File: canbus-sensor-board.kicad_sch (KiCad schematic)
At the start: 48 parts, among them J1 CAN IO, J2 CAN Term, J3 POWER IN, J4 Debug, J5 I2C2 IO, J6 I2C1 IO, Q1 2N7002, Q2 2N7002, Q3 2N7002, Q4 2N7002, SW1 Reset, SW2 Boot, U1 MCP2551-I-SN, U3 AMS1117-3.3, U4 STM32F103C8Tx

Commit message: Update board to rev 3 (we do not talk about rev 2)
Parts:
- removed J4: Debug, Connector_PinHeader_2.54mm:PinHeader_1x04_P2.54mm_Vertical, symbol Connector:Conn_01x04_Pin
- removed SW1: Reset, Button_Switch_SMD:SW_Push_1P1T_XKB_TS-1187A, symbol Switch:SW_SPST
- removed SW2: Boot, Button_Switch_SMD:SW_Push_1P1T_XKB_TS-1187A, symbol Switch:SW_SPST
- added J10, J11, J4, J7, J9: Conn_01x01, Connector_Wire:SolderWirePad_1x01_SMD_1x2mm, symbol Connector_Generic:Conn_01x01
- added J8: Conn_ARM_SWD_TagConnect_TC2030-NL, Connector:Tag-Connect_TC2030-IDC-NL_2x03_P1.27mm_Vertical, symbol Connector:Conn_ARM_SWD_TagConnect_TC2030-NL
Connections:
- net +3.3V: now also R3.2, J11.1 (Pin_1), J8.1 (VCC); no longer R3.1
- net +5V: now also J4.1 (Pin_1)
- net BOOT: now also J7.1 (Pin_1)
- net CAN_RX: now also U4.45 (PB8); no longer U4.29 (PA8)
- net CAN_TX: now also U4.46 (PB9); no longer U4.30 (PA9)
- net DEBUG_LED1: now also U4.38 (PA15); no longer U4.37 (PA14)
- net GND: now also J10.1 (Pin_1), J8.5 (GND)
- net NRST: now also R3.1, J8.3 (~{RESET}), J9.1 (Pin_1); no longer R3.2
- net SWDIO: now reaches U4.34 (PA13)
- net SWDIO: now also J8.2 (SWDIO)
- net SWO: now reaches U4.39 (PB3)
- net SWO: now also J8.6 (SWO)
- net SYS_SWCLK: no longer names the net of U4.32 (PA11)
- net SYS_SWDIO: no longer names the net of U4.31 (PA10)
- new net SWCLK: J8.4 (SWCLK), U4.37 (PA14)
- no-connect marks 27 -> 26

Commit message: Switch to MOSFETs with lower Vgs thresholds
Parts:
- removed Q1, Q2, Q3, Q4: 2N7002, Package_TO_SOT_SMD:SOT-23, symbol Transistor_FET:2N7002
- added Q1, Q2, Q3, Q4: AO3400A, Package_TO_SOT_SMD:SOT-23, symbol Transistor_FET:AO3400A
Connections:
- net +3.3V: now also Q1.1 (G), Q2.1 (G), Q3.1 (G), Q4.1 (G)
- net I2C1_SCL: now also Q1.2 (S)
- net I2C1_SCL_5V: now also Q1.3 (D)
- net I2C1_SDA: now also Q2.2 (S)
- net I2C1_SDA_5V: now also Q2.3 (D)
- net I2C2_SCL: now also Q3.2 (S)
- net I2C2_SCL_5V: now also Q3.3 (D)
- net I2C2_SDA: now also Q4.2 (S)
- net I2C2_SDA_5V: now also Q4.3 (D)

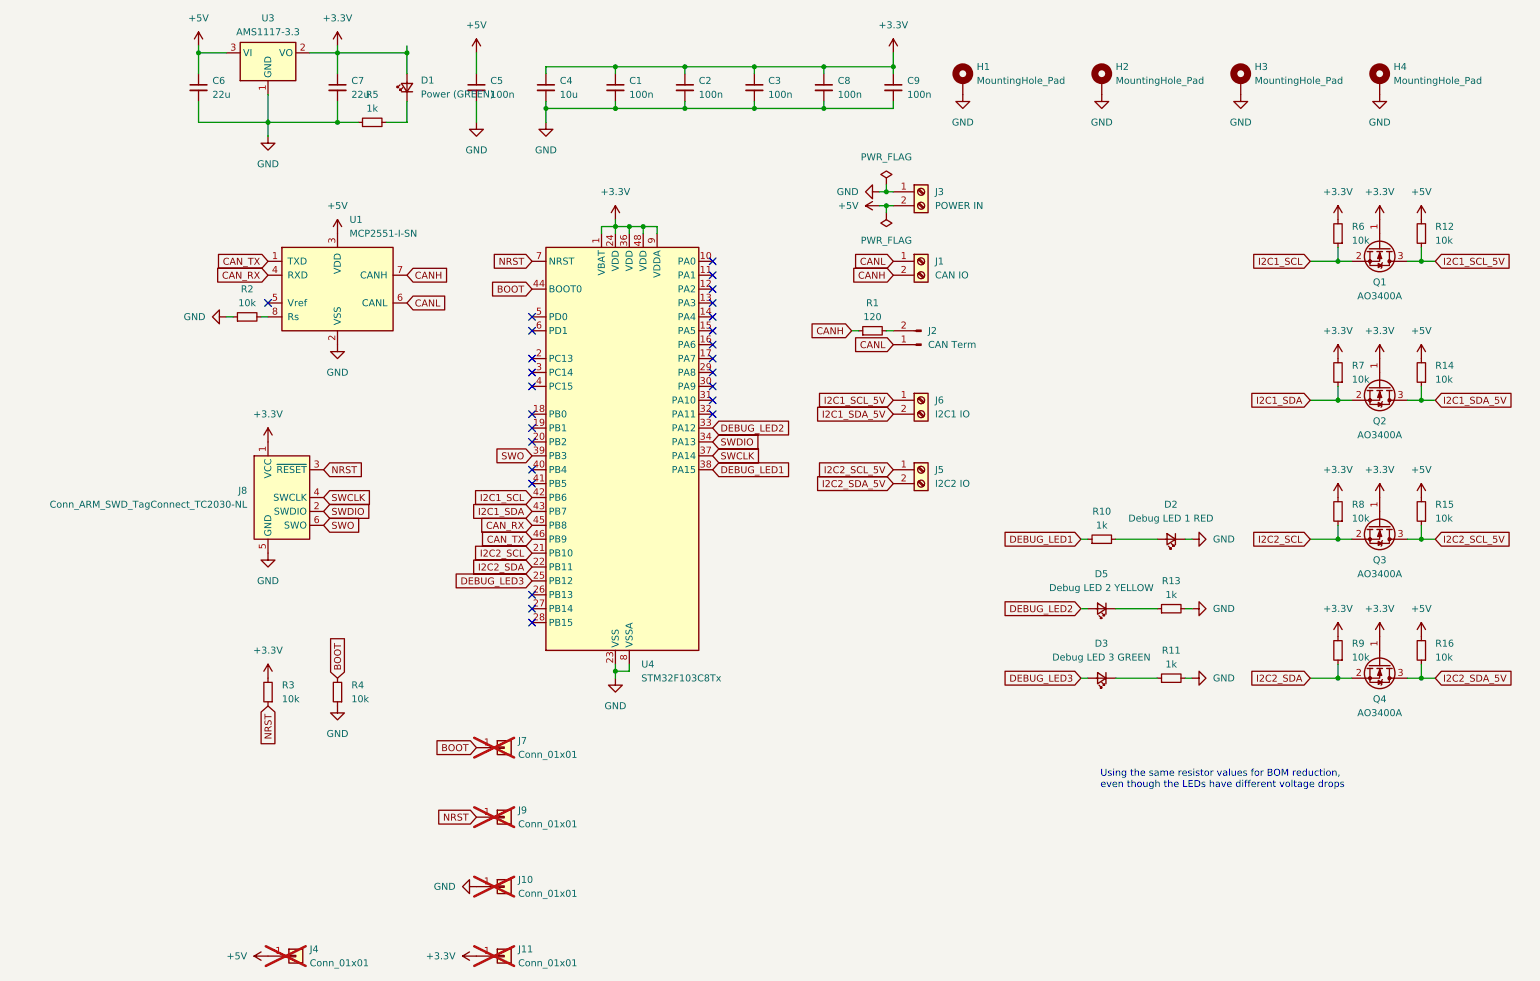
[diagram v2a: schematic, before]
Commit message: Further tweak rev4 of the board
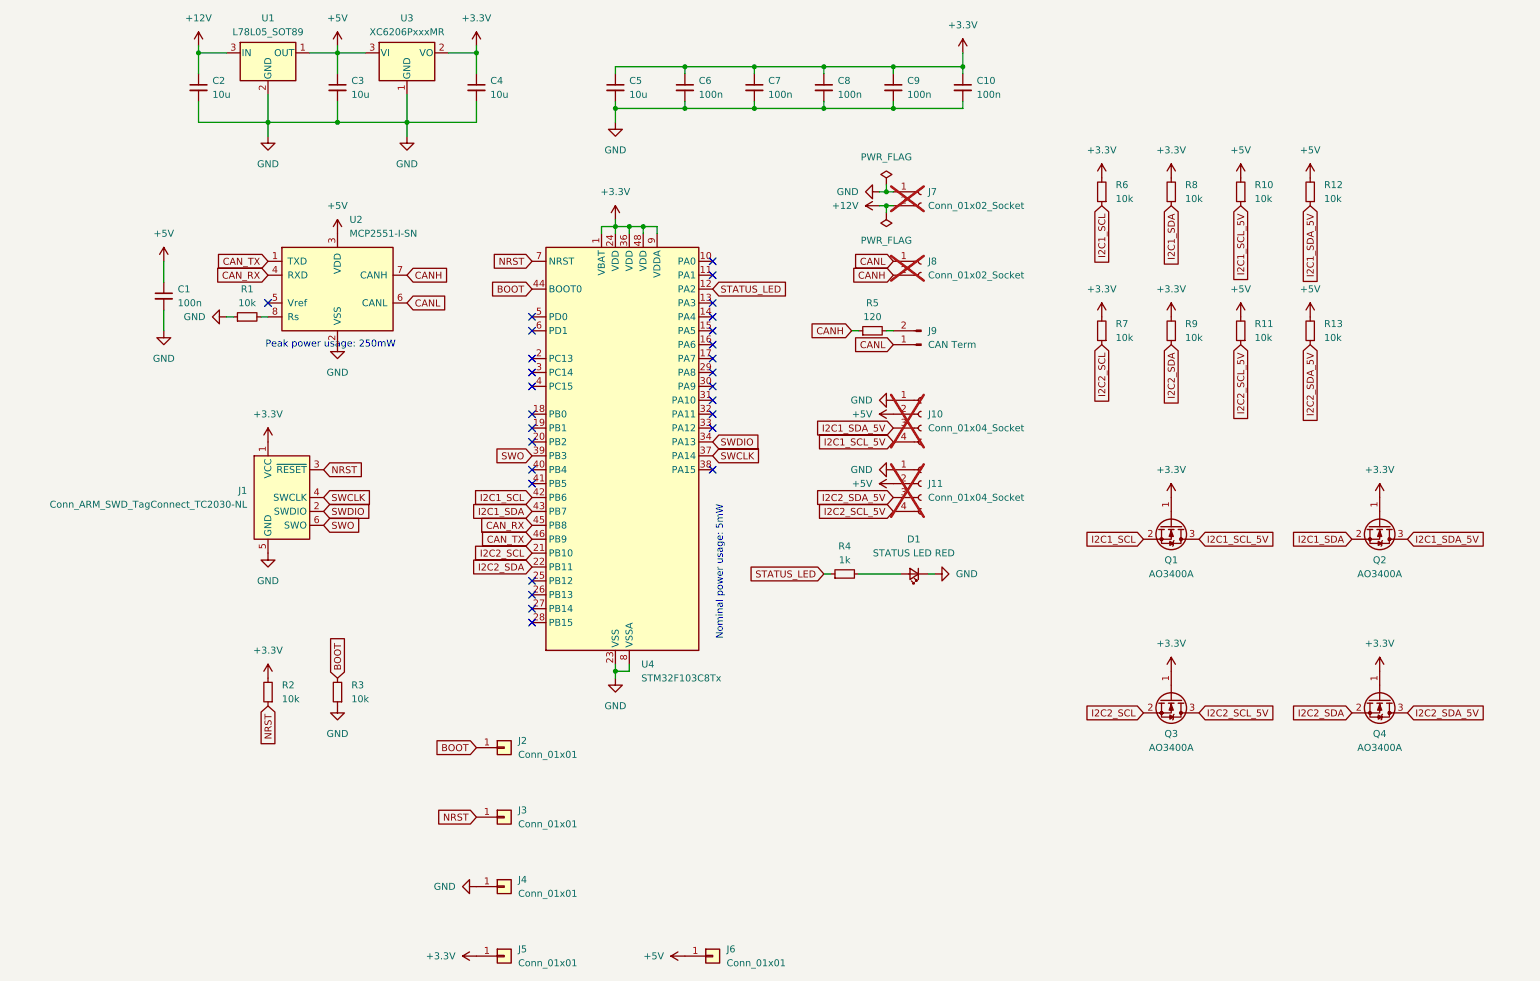
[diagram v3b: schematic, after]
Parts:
- removed D1: Power (GREEN), LED_SMD:LED_0805_2012Metric, symbol Device:LED_Small
- removed D3: Debug LED 3 GREEN, LED_SMD:LED_0805_2012Metric, symbol Device:LED_Small
- removed D5: Debug LED 2 YELLOW, LED_SMD:LED_0805_2012Metric, symbol Device:LED_Small
- removed H1, H2, H3, H4: MountingHole_Pad, MountingHole:MountingHole_2.2mm_M2_Pad, symbol Mechanical:MountingHole_Pad
- removed J1: CAN IO, TerminalBlock_4Ucon:TerminalBlock_4Ucon_1x02_P3.50mm_Horizontal, symbol Connector:Screw_Terminal_01x02
- removed J3: POWER IN, TerminalBlock_4Ucon:TerminalBlock_4Ucon_1x02_P3.50mm_Horizontal, symbol Connector:Screw_Terminal_01x02
- removed J4: Conn_01x01, Connector_Wire:SolderWirePad_1x01_SMD_1x2mm, symbol Connector_Generic:Conn_01x01
- removed J5: I2C2 IO, TerminalBlock_4Ucon:TerminalBlock_4Ucon_1x02_P3.50mm_Horizontal, symbol Connector:Screw_Terminal_01x02
- removed J6: I2C1 IO, TerminalBlock_4Ucon:TerminalBlock_4Ucon_1x02_P3.50mm_Horizontal, symbol Connector:Screw_Terminal_01x02
- removed R14, R15, R16: 10k, Resistor_SMD:R_0402_1005Metric, symbol Device:R_Small
- removed R5: 1k, Resistor_SMD:R_0402_1005Metric, symbol Device:R_Small
- removed U3: AMS1117-3.3, Package_TO_SOT_SMD:SOT-223-3_TabPin2, symbol Regulator_Linear:AMS1117-3.3
- added C2: 10u, Capacitor_SMD:C_0402_1005Metric, symbol Device:C_Small
- added J10, J11: Conn_01x04_Socket, Connector_PinHeader_2.00mm:PinHeader_1x04_P2.00mm_Vertical, symbol Connector:Conn_01x04_Socket
- added J6: Conn_01x01, TestPoint:TestPoint_Pad_D1.0mm, symbol Connector_Generic:Conn_01x01
- added J7, J8: Conn_01x02_Socket, Connector_PinHeader_2.00mm:PinHeader_1x02_P2.00mm_Vertical, symbol Connector:Conn_01x02_Socket
- added R10: 10k, Resistor_SMD:R_0402_1005Metric, symbol Device:R_Small
- added U1: L78L05_SOT89, Package_TO_SOT_SMD:SOT-89-3, symbol Regulator_Linear:L78L05_SOT89
- added U3: XC6206PxxxMR, Package_TO_SOT_SMD:SOT-23-3, symbol Regulator_Linear:XC6206PxxxMR
- C3: renamed from C6; value 22u -> 10u; footprint Capacitor_SMD:C_1206_3216Metric -> Capacitor_SMD:C_0402_1005Metric; MPN C12891 -> C15525
- C4: renamed from C7; value 22u -> 10u; footprint Capacitor_SMD:C_1206_3216Metric -> Capacitor_SMD:C_0402_1005Metric; MPN C12891 -> C15525
- C5: renamed from C4; footprint Capacitor_SMD:C_0805_2012Metric -> Capacitor_SMD:C_0402_1005Metric; MPN C15850 -> C15525
- D1: renamed from D2; value Debug LED 1 RED -> STATUS LED RED; footprint LED_SMD:LED_0805_2012Metric -> LED_SMD:LED_0603_1608Metric; MPN C84256 -> C2286
- J2: renamed from J7; footprint Connector_Wire:SolderWirePad_1x01_SMD_1x2mm -> TestPoint:TestPoint_Pad_D1.0mm; now fitted
- J3: renamed from J9; footprint Connector_Wire:SolderWirePad_1x01_SMD_1x2mm -> TestPoint:TestPoint_Pad_D1.0mm; now fitted
- J4: renamed from J10; footprint Connector_Wire:SolderWirePad_1x01_SMD_1x2mm -> TestPoint:TestPoint_Pad_D1.0mm; now fitted
- J5: renamed from J11; footprint Connector_Wire:SolderWirePad_1x01_SMD_1x2mm -> TestPoint:TestPoint_Pad_D1.0mm; now fitted
- J9: renamed from J2; footprint Connector_PinHeader_2.54mm:PinHeader_1x02_P2.54mm_Vertical -> Jumper:SolderJumper-2_P1.3mm_Open_Pad1.0x1.5mm; MPN C492401 -> (none)
- Q1, Q2, Q3, Q4: MPN (none) -> C20917
- R11, R13: value 1k -> 10k; MPN C11702 -> C25744
- renumbered C5 to C1, C9 to C10, C1 to C6, C2 to C7, C3 to C8, C8 to C9, J8 to J1, R2 to R1, R3 to R2, R4 to R3, R10 to R4, R1 to R5, R8 to R7, R7 to R8, U1 to U2
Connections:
- net +3.3V: now also U3.2 (VO)
- net +5V: now also R11.2, R13.2, J10.2 (Pin_2), J11.2 (Pin_2), J6.1 (Pin_1), R10.2, U1.1 (OUT), U3.3 (VI)
- net CANH: now also J8.2 (Pin_2)
- net CANL: now also J8.1 (Pin_1)
- net GND: now also C2.2, J10.1 (Pin_1), J11.1 (Pin_1), J7.1 (Pin_1), U1.2 (GND), U3.1 (GND); no longer R11.2, R13.2
- net I2C1_SCL_5V: now also J10.4 (Pin_4), R10.1; no longer R12.1
- net I2C1_SDA_5V: now also R12.1, J10.3 (Pin_3)
- net I2C2_SCL_5V: now also R11.1, J11.4 (Pin_4)
- net I2C2_SDA_5V: now also R13.1, J11.3 (Pin_3)
- net STATUS_LED: now reaches U4.12 (PA2)
- net STATUS_LED: now also R4.1
- net DEBUG_LED1: no longer names the net of U4.38 (PA15)
- net DEBUG_LED1: no longer R4.1
- net DEBUG_LED2: no longer names the net of U4.33 (PA12)
- net DEBUG_LED3: no longer names the net of U4.25 (PB12)
- new net +12V: C2.1, J7.2 (Pin_2), U1.3 (IN)
- no-connect marks 26 -> 28
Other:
- note added: "Nominal power usage: 5mW"
- note added: "Peak power usage: 250mW"
- note removed: "Using the same resistor values for BOM reduction, even though the LEDs have different voltage drops"
- moved on the sheet: C1, C10, C3, C4, C5, C6, C7, C8, C9, D1, R4, R6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

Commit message: Increase 12-24V cap size so it actually handles that voltage range
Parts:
- C1: renamed from C2; value 10u -> 10u >24V; footprint Capacitor_SMD:C_0402_1005Metric -> Capacitor_SMD:C_0805_2012Metric; MPN C15525 -> C440198
- renumbered C1 to C10, C3 to C2, C4 to C3, C5 to C4, C6 to C5, C7 to C6, C8 to C7, C9 to C8, C10 to C9, J9 to J2, J2 to J3, J3 to J4, J4 to J5, J5 to J6, J6 to J7, J7 to J8, J8 to J9, Q3 to Q2, Q2 to Q3, R4 to R1, R5 to R2, R2 to R3, R3 to R4, R1 to R5, U3 to U2, U4 to U3, U2 to U4
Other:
- moved on the sheet: C10, D1, J1, J2, R1, R2, R3, R4, R5, U4

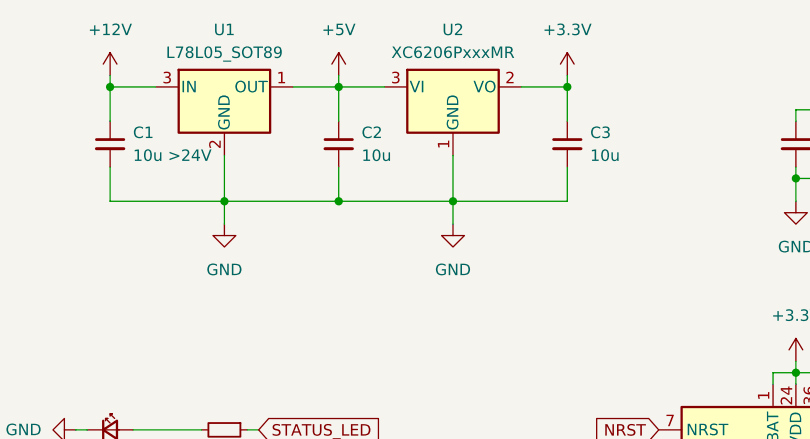
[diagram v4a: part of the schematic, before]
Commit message: Also make 5V cap larger to have more error margin
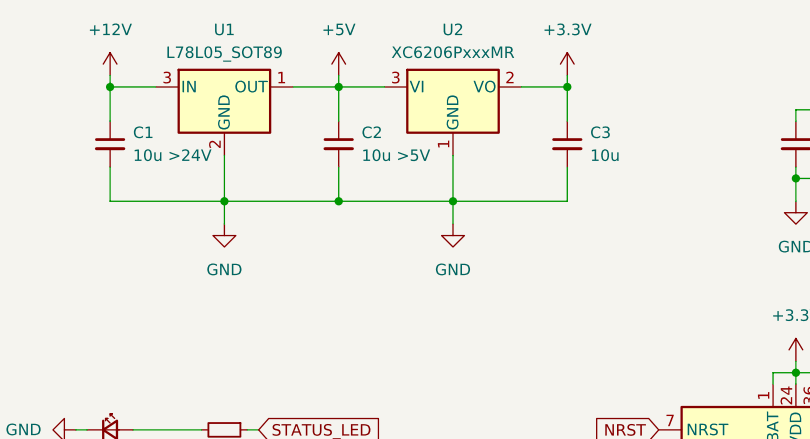
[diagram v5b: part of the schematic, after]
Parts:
- C2: value 10u -> 10u >5V; footprint Capacitor_SMD:C_0402_1005Metric -> Capacitor_SMD:C_0603_1608Metric; MPN C15525 -> C19702
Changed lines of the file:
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@@
 			)
 		)
-		(property "Value" "10u"
+		(property "Value" "10u >5V"
 			(at 66.04 33.0262 0)
 			(effects
@@
 			)
 		)
-		(property "Footprint" "Capacitor_SMD:C_0402_1005Metric"
+		(property "Footprint" "Capacitor_SMD:C_0603_1608Metric"
 			(at 63.5 31.75 0)
 			(effects
@@
 			)
 		)
-		(property "MPN" "C15525"
+		(property "MPN" "C19702"
 			(at 63.5 31.75 0)
 			(effects
